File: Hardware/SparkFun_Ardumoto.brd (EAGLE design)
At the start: 59.7 x 53.3 mm, 64 parts, among them U1 ARDUINO, U2 L298, U5 74HC1G04, U6 74HC1G04

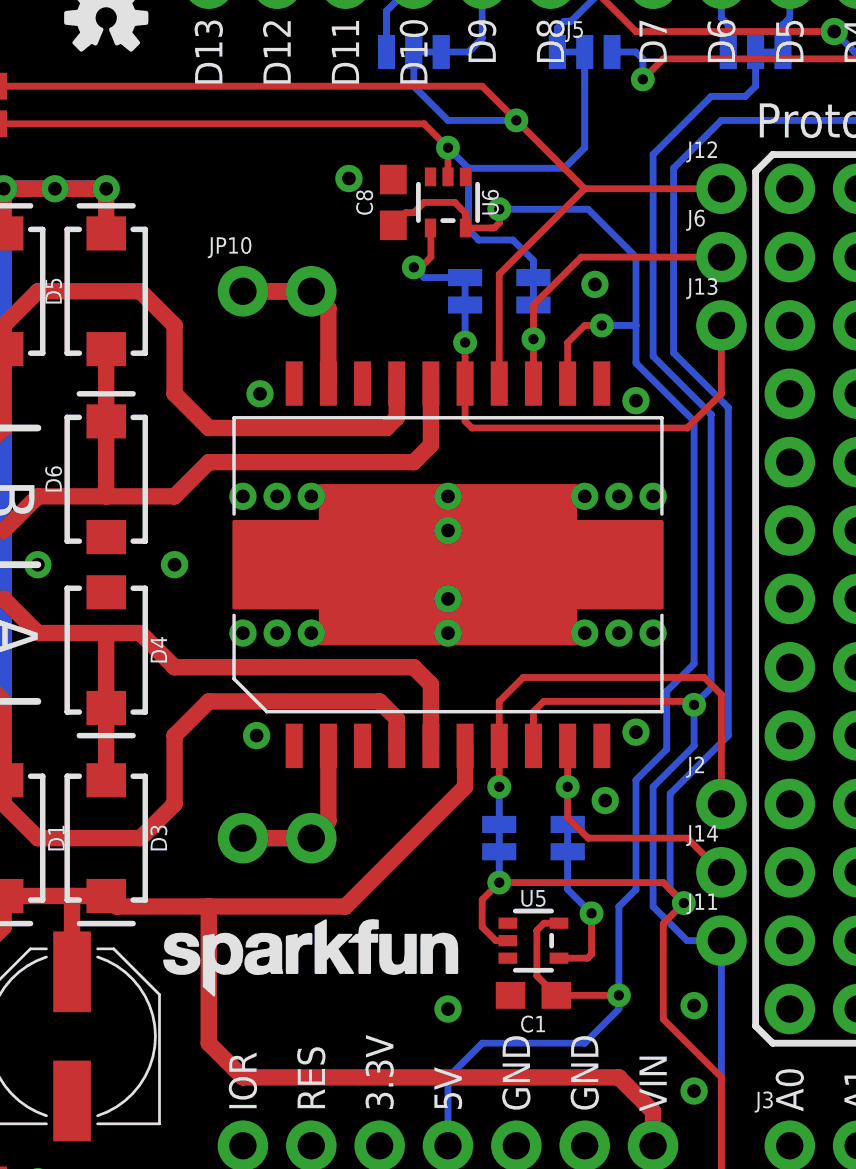
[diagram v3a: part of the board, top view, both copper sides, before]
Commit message: Touched up the silk a bit in preparation for review
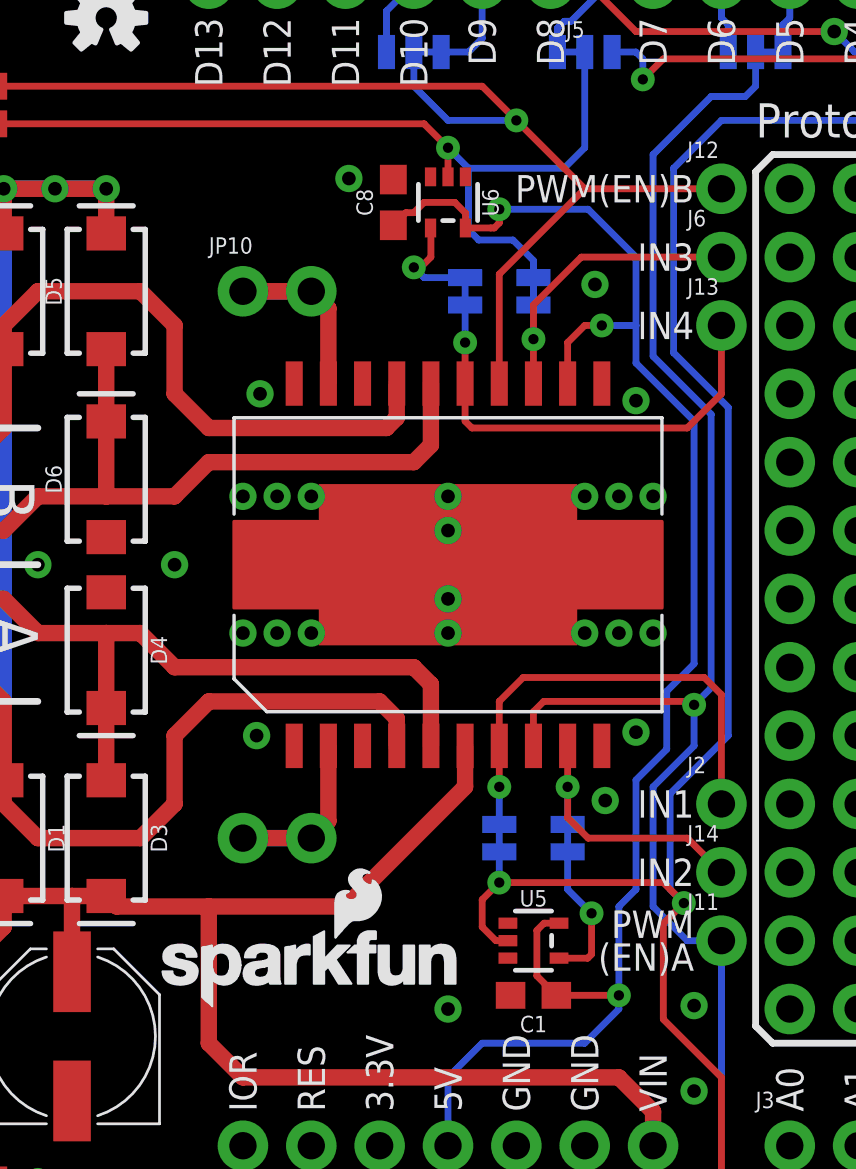
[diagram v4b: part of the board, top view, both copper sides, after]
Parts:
- LOGO2: value SFE_LOGO_NAME.1_INCH -> SFE_LOGO_NAME_FLAME.1_INCH; device SparkFun-Aesthetics:SFE_LOGO_NAME_.1 -> SparkFun-Aesthetics:SFE_LOGO_NAME_FLAME_.1
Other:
- board text added: "PWM (EN)A"

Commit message: Going for QC inspection
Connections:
- net N$11 renamed SENB
- net N$14 renamed SENA
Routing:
- net SENB: track 8.77 -> 6.23 mm
- net SENA: track 8.77 -> 6.23 mm
- net GND: vias 36 -> 45
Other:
- board text added: "ISOLATE"
- board text added: "Pete Dokter"
- board text added: "RX"
- board text added: "Revised by: Marshall Taylor"
- board text added: "SENSE A"
- board text added: "SENSE B"
- board text added: "TX"
- board text removed: "DISCONNECTS"

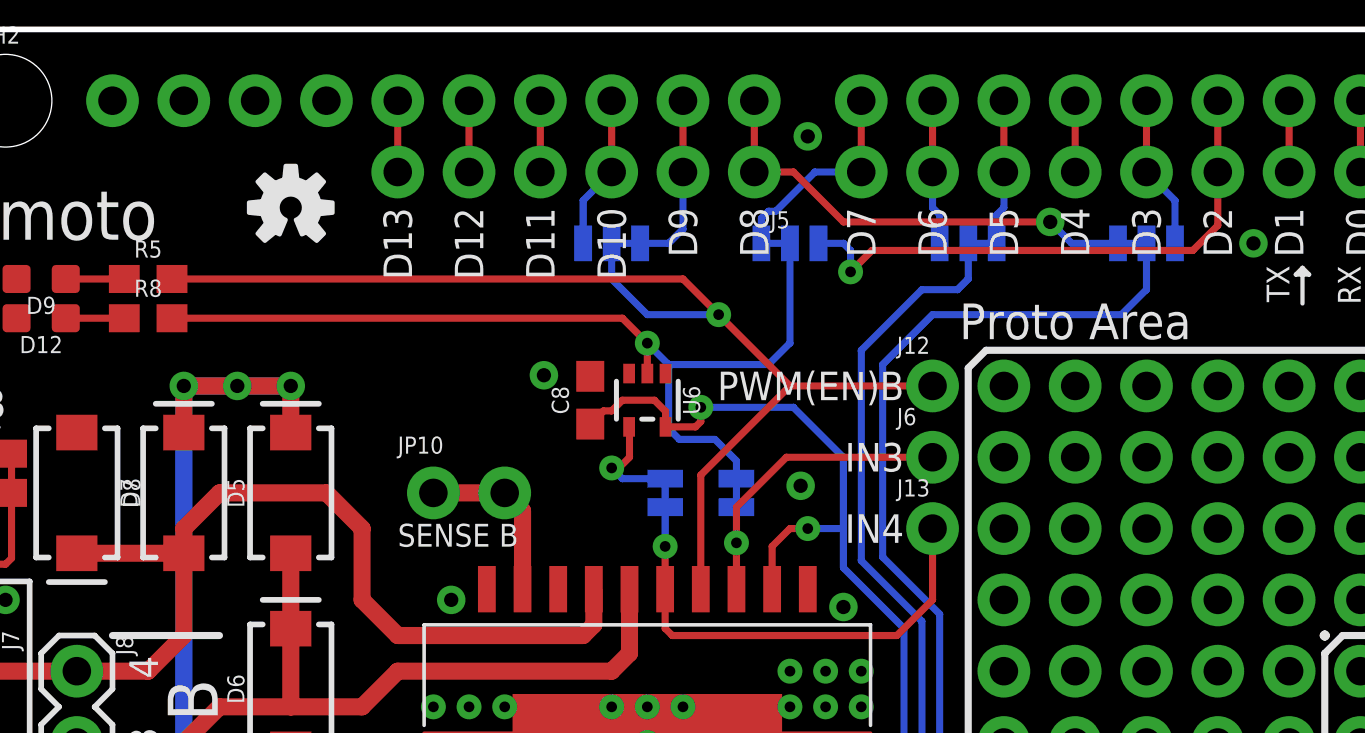
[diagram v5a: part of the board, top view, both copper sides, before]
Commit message: Reordered two R3 pins (9 and 6).  Switched sheet locations and adjusted logos.  Removed invalid airwires
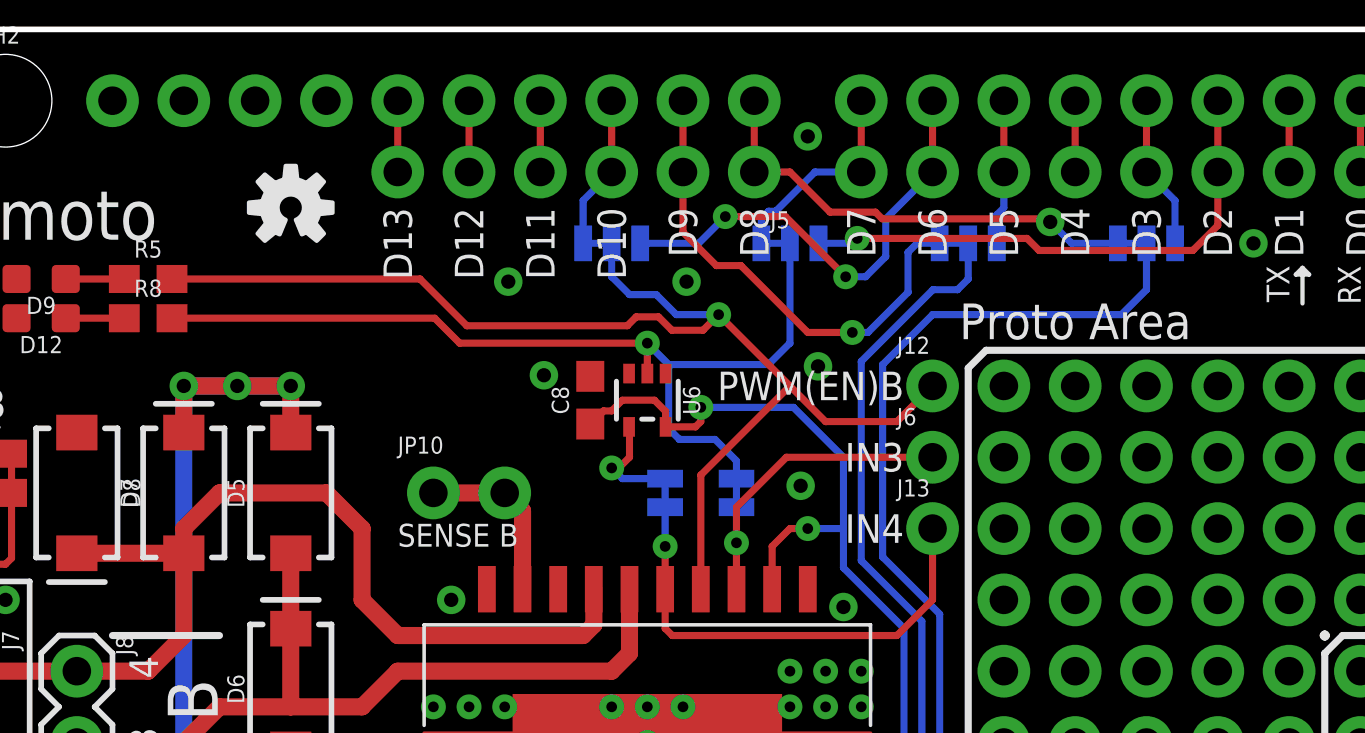
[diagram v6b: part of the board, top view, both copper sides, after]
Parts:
- moved FRAME1 5.08 mm to (-2.56, -15.2)
- turned JP2 to 0 degrees
- turned JP4 to 0 degrees
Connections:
- net D10: now also JP4.3; no longer JP4.1
- net D5: now also JP2.1; no longer JP2.3
- net D6: now also JP4.1; no longer JP2.1
- net D9: now also JP2.3; no longer JP4.3
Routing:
- net D6: track 5.19 -> 16.6 mm, vias 0 -> 2
- net D9: track 6.31 -> 17.5 mm, vias 0 -> 1
- net PWMB: track 42.8 -> 44.6 mm
- net D2: track 20.2 -> 19.3 mm
- net GND: vias 45 -> 48
